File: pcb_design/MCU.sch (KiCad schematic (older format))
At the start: 17 parts, among them J9 SWD, SW1 BOOTLOADER, U1 STM32F40X_LQFP64, X2 ABM3B - 8MHz

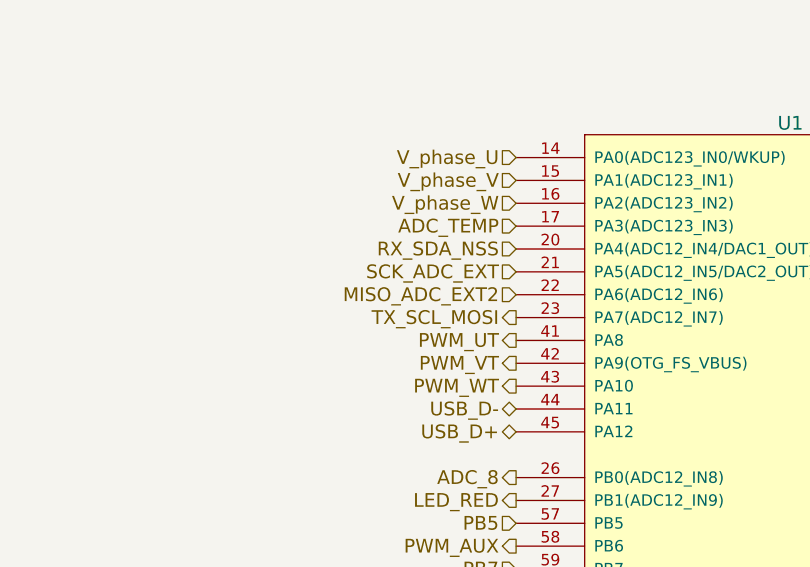
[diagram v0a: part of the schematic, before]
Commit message: Added individual temperature sensing for each half bridge and 2 pwm gpio with low side driver
Signed-off-by: Marcos Chaparro <mchaparro@paltatech.com>
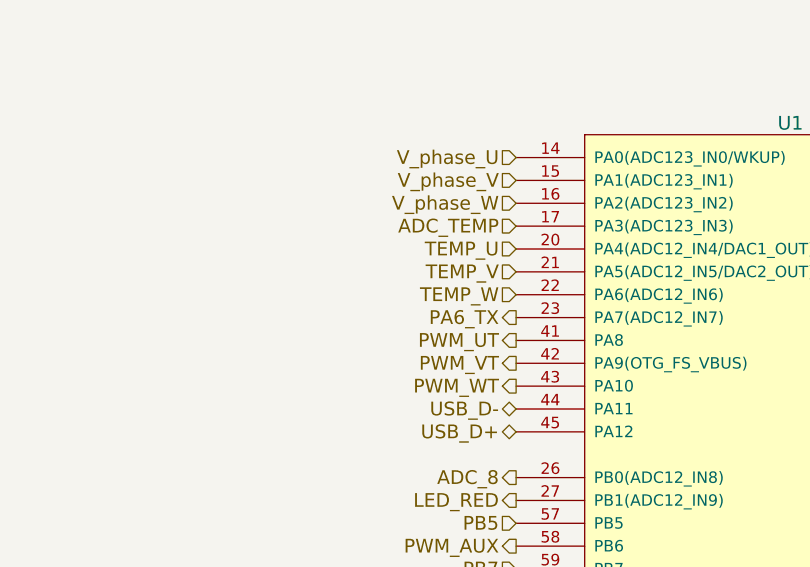
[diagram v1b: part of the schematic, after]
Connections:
- net RX_SDA_NSS: no longer U1.20 (PA4(ADC12_IN4/DAC1_OUT))
- net TX_SCL_MOSI: no longer U1.23 (PA7(ADC12_IN7))
- net MISO_ADC_EXT2 renamed TEMP_W
- net SCK_ADC_EXT renamed TEMP_V
- new net PA6_TX: U1.23 (PA7(ADC12_IN7))
- new net TEMP_U: U1.20 (PA4(ADC12_IN4/DAC1_OUT))
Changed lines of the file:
@@
 $Descr A4 11693 8268
 encoding utf-8
-Sheet 12 14
+Sheet 13 15
 Title "VESC 6.4"
 Date "2017-02-22"
@@
 PWM_UB
 Text HLabel 3650 2000 0    60   Input ~ 0
-SCK_ADC_EXT
+TEMP_V
 Text HLabel 3650 3800 0    60   Input ~ 0
 ~FAULT
@@
 LED_GREEN
 Text HLabel 3650 2100 0    60   Input ~ 0
-MISO_ADC_EXT2
+TEMP_W
 Text HLabel 3650 2200 0    60   Output ~ 0
-TX_SCL_MOSI
+PA6_TX
 Text HLabel 3650 1800 0    60   Input ~ 0
 ADC_TEMP
@@
 Text HLabel 3650 3100 0    60   Input ~ 0
 PB5
-Text HLabel 3650 1900 0    60   Input ~ 0
-RX_SDA_NSS
 Wire Wire Line
 	6150 5200 6350 5200
@@
 Text Notes 750  3950 0    60   ~ 12
 Changes for board support package
+Text HLabel 3650 1900 0    60   Input ~ 0
+TEMP_U
 $EndSCHEMATC

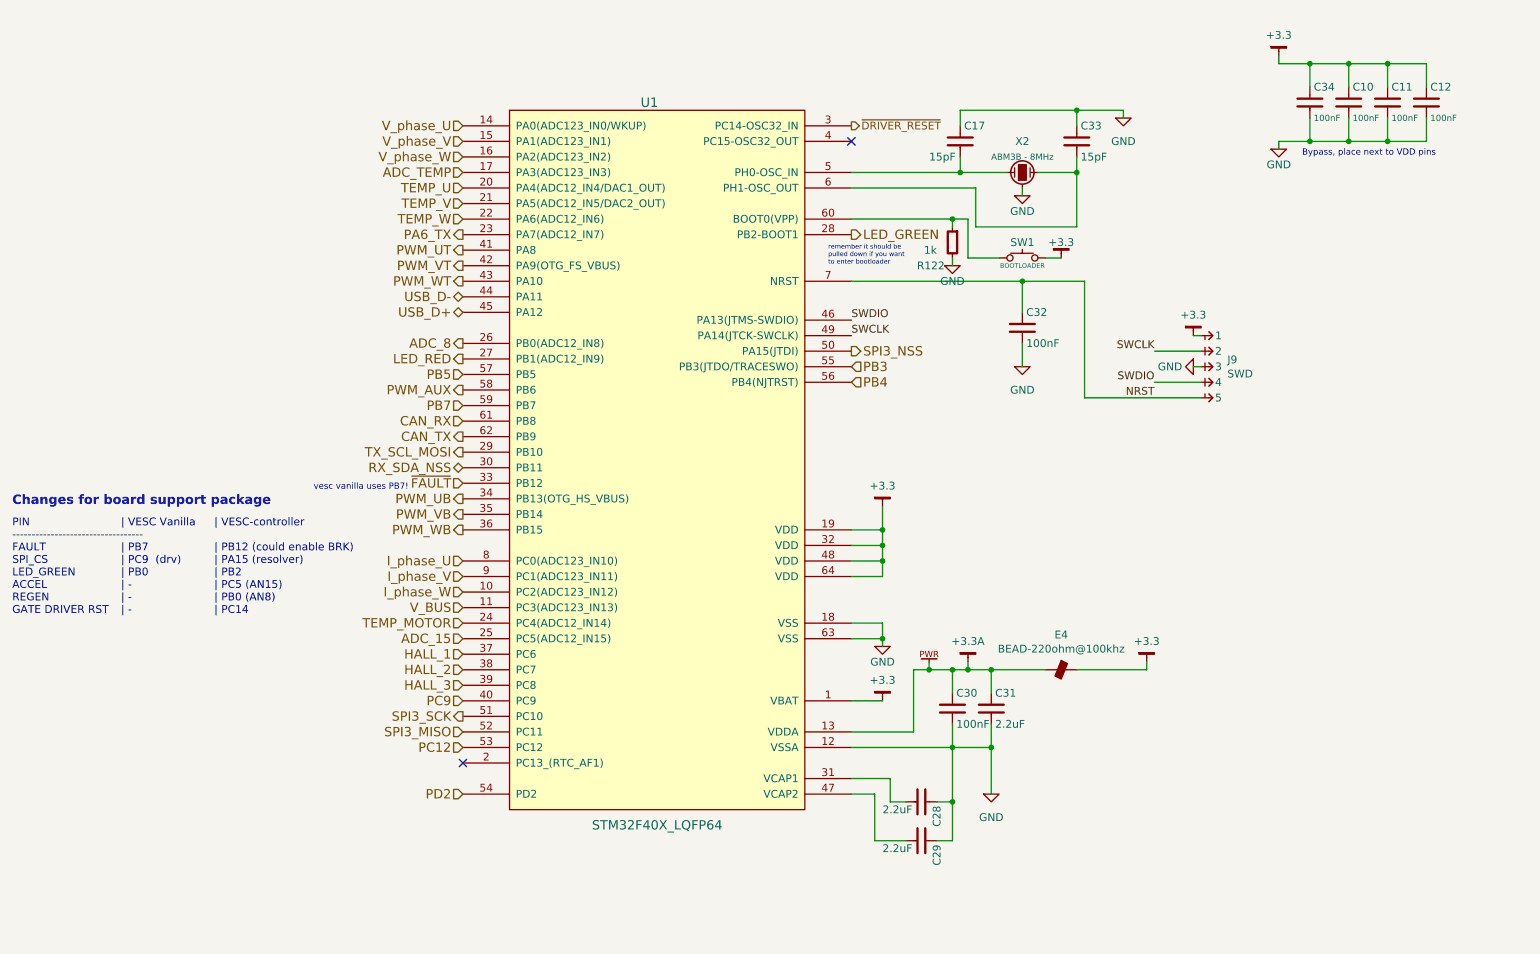
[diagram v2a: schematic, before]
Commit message: Added RC filter to FAULT line to prevent noise triggering it
Signed-off-by: Marcos Chaparro <mchaparro@paltatech.com>
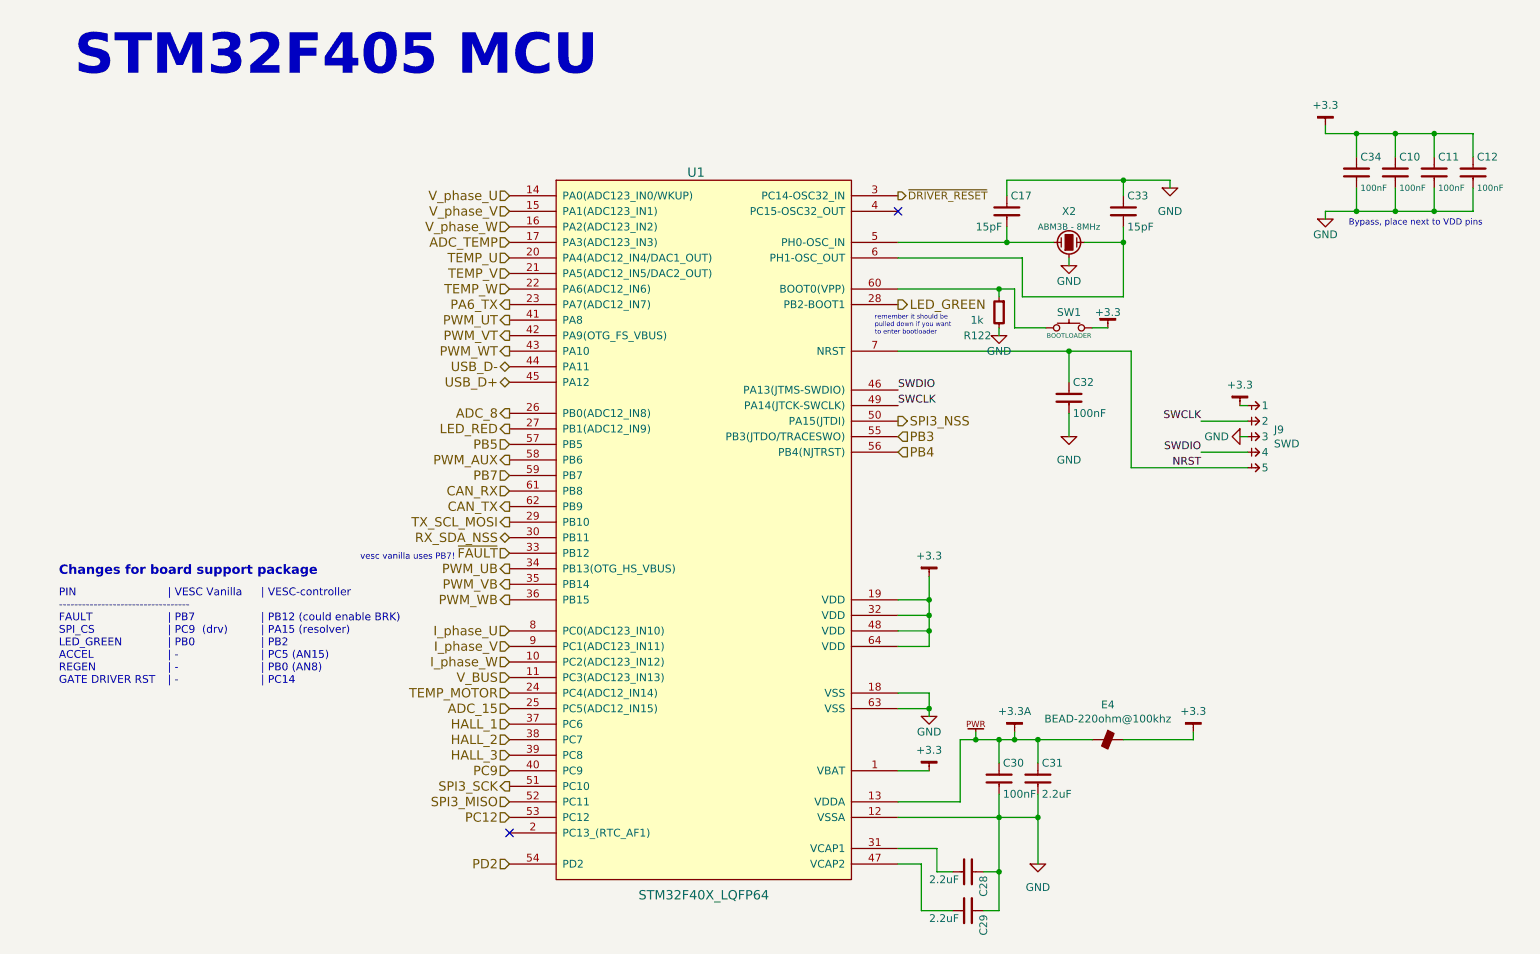
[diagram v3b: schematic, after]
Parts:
- C10, C11, C12, C30, C32: BOM (none) -> CAP MLCC 100nF C0G 50V 5% [0603]
- C28, C29, C31: BOM (none) -> CAP MLCC 100pF C0G 50V 5% [0603]
- C34: BOM CAP MLCC 100pF C0G 50V 5% [0603] -> CAP MLCC 100nF C0G 50V 5% [0603]
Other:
- note added: "STM32F405 MCU"
- moved on the sheet: C10, C11, C12, C17, C28, C29, C30, C31, C32, C33, C34, E4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
